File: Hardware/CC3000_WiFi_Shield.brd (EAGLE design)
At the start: 66 x 53.3 mm, 37 parts, among them J1 U.FL, U2 ARDUINO_SHIELDNOLABELS, U3 74HC4050, U4 USD-SOCKETNEW, U5 CC3000, U6 74AHC1G125

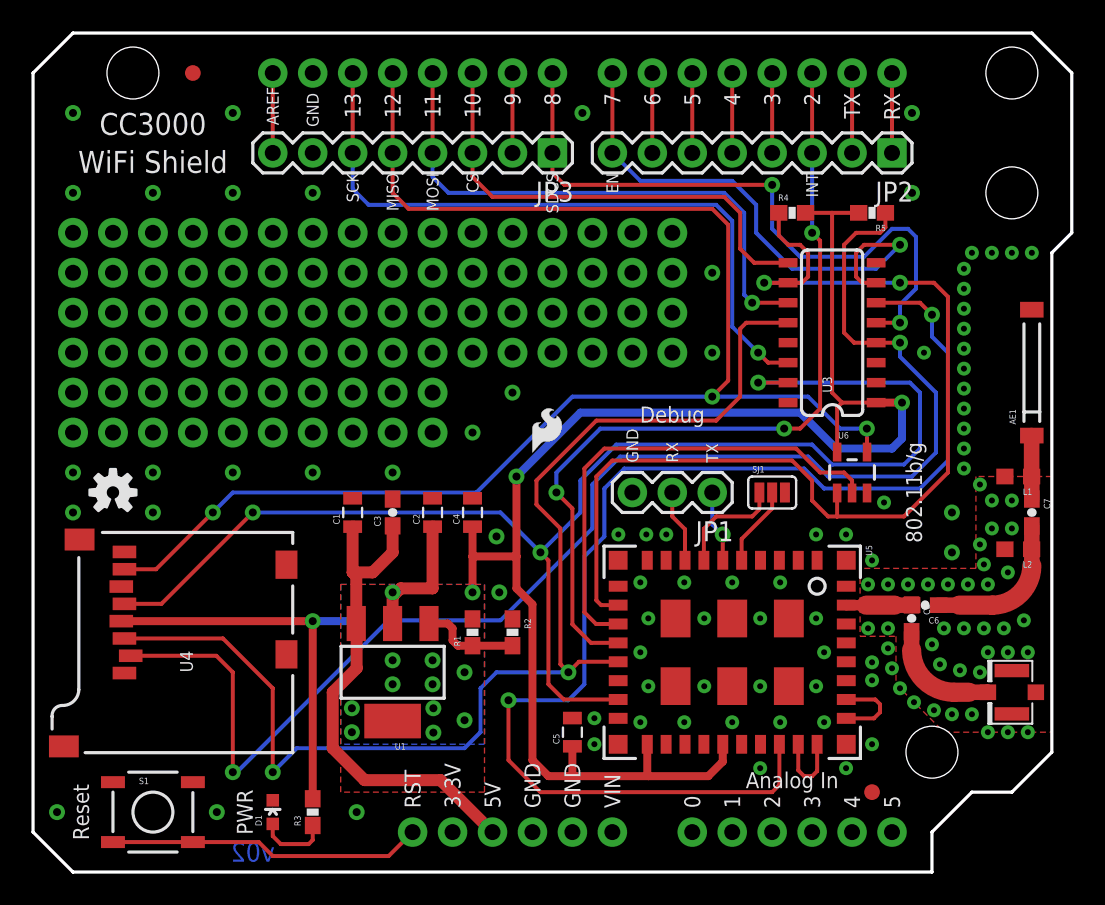
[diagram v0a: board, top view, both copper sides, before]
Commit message: Added power breakout near proto area. Removed silk from shield headers. Changed silk text to 0.032 in. size. Added ISP headers to work with Leonardo. Added 10-pin shield headers to work woth UNO R3. Adjusted notch on bottom-right corner of board.
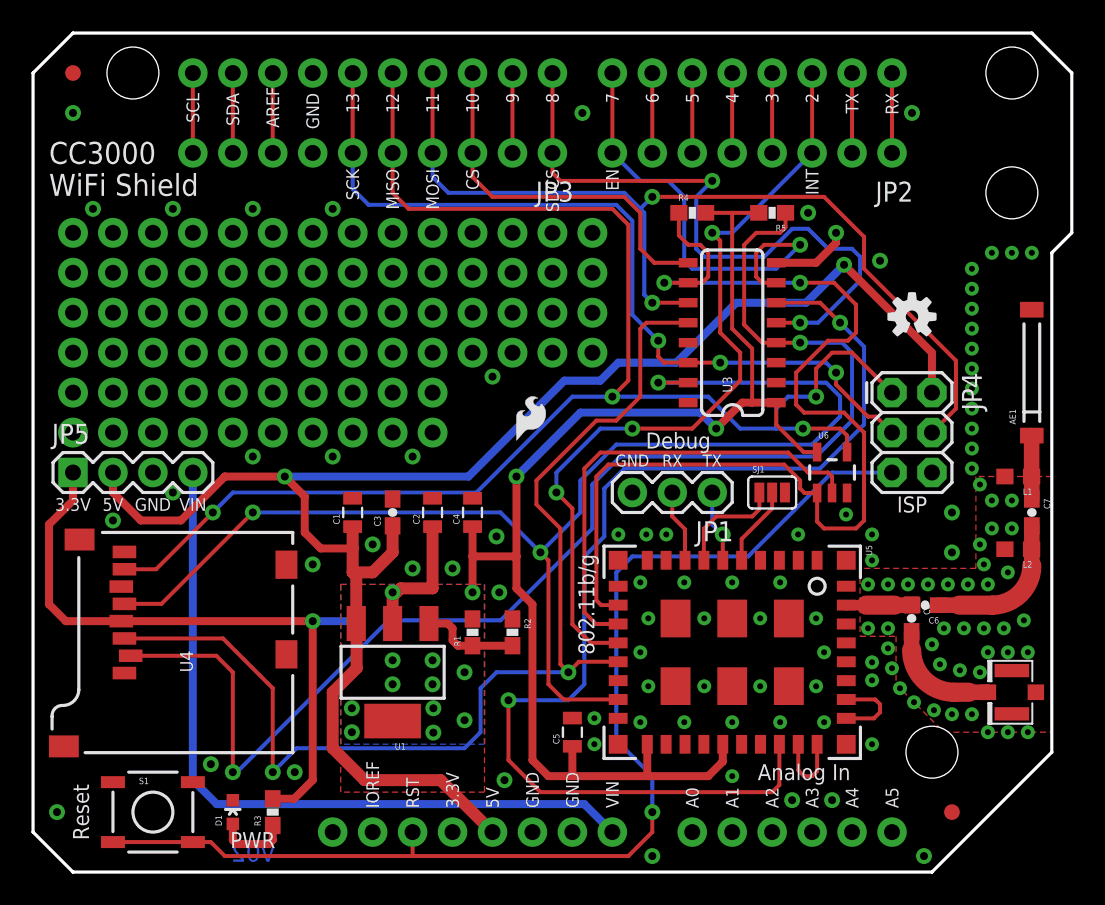
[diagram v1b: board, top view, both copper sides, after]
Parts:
- added JP4: AVR_SPI_PRG_6PTH, SparkFun-Connectors:2X3
- added JP5: (no value), SparkFun-Connectors:1X04
- JP2: device SparkFun-Connectors:1X08 -> SparkFun-Connectors:1X08_NO_SILK
- JP3: value (none) -> M10NO_SILK; device SparkFun-Connectors:1X08 -> SparkFun-Connectors:1X10_NO_SILK
- U2: value ARDUINO_SHIELDNOLABELS -> ARDUINO_R3_SHIELDNOLABELS; device SparkFun-Boards:DUEMILANOVE_SHIELD_NOLABELS -> SparkFun-Boards:UNO_R3_SHIELD_NOLABELS
- moved LOGO1 52.0 mm to (55.9, 35.3)
- moved FID2 7.62 mm to (2.54, 50.8)
- moved R4 6.35 mm to (41.9, 41.9)
- moved R5 6.35 mm to (47.0, 41.9)
- moved U3 6.35 mm to (44.5, 34.3)
- moved FID1 5.24 mm to (58.4, 3.81)
- moved D1 2.54 mm to (12.7, 3.81)
- moved R3 2.54 mm to (15.2, 3.81)
- moved U6 1.27 mm to (50.8, 25.4)
- moved LOGO3 1.27 mm to (30.7, 27.4)
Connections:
- removed net N$1: S1.3, S1.4, U2.RES
- new net RESET: JP4.5, S1.3, S1.4, U2.RES
- new net SCL: JP3.10, U2.SCL
- new net SDA: JP3.9, U2.SDA
- new net VIN: JP5.4, U2.VIN
- net 3.3V: now also JP5.1
- net 5V: now also JP4.2, JP5.2
- net GND: now also JP4.6, JP5.3
- net MISO_3.3V: now also JP4.1
- net MOSI_5V: now also JP4.4
- net SCK_5V: now also JP4.3
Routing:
- net RESET: track 0.00 -> 74.4 mm, vias 0 -> 1
- net 5V: track 31.9 -> 105.2 mm, vias 0 -> 2
- net VIN: track 0.00 -> 47.6 mm
- net MOSI_5V: track 35.6 -> 60.3 mm, vias 1 -> 2
- net N$1: track 20.0 -> 0.00 mm
- net SCK_5V: track 43.7 -> 52.8 mm, vias 1 -> 3
- net EN_3.3V: track 80.1 -> 72.8 mm
- net CS_5V: track 30.3 -> 23.9 mm
- net MOSI_3.3V: track 78.3 -> 71.9 mm
- net SCK_3.3V: track 88.4 -> 82.2 mm
- net SD_CS_3.3V: track 90.4 -> 84.5 mm
- net SDA: track 0.00 -> 5.08 mm
- net SCL: track 0.00 -> 5.08 mm
- net EN_5V: track 34.1 -> 29.0 mm
- net GND: track 0.00 -> 4.97 mm, vias 115 -> 117
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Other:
- outline, holes or cut-outs redrawn
- board text added: "A0"
- board text added: "A1"
- board text added: "A2"
- board text added: "A3"
- board text added: "A4"
- board text added: "A5"
- board text added: "IOREF"
- board text added: "ISP"
- board text added: "SCL"
- board text added: "SDA"
- board text removed: "0"
- board text removed: "1"

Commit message: Moved ext antenna mount back 50 mil; re-routed SD_CS line to avoid splitting power plane on bottom; Added 'Antenna Select' to SS; Added SS marker to U.FL; Added 'Mode' in SS to jumper; Changed to v10
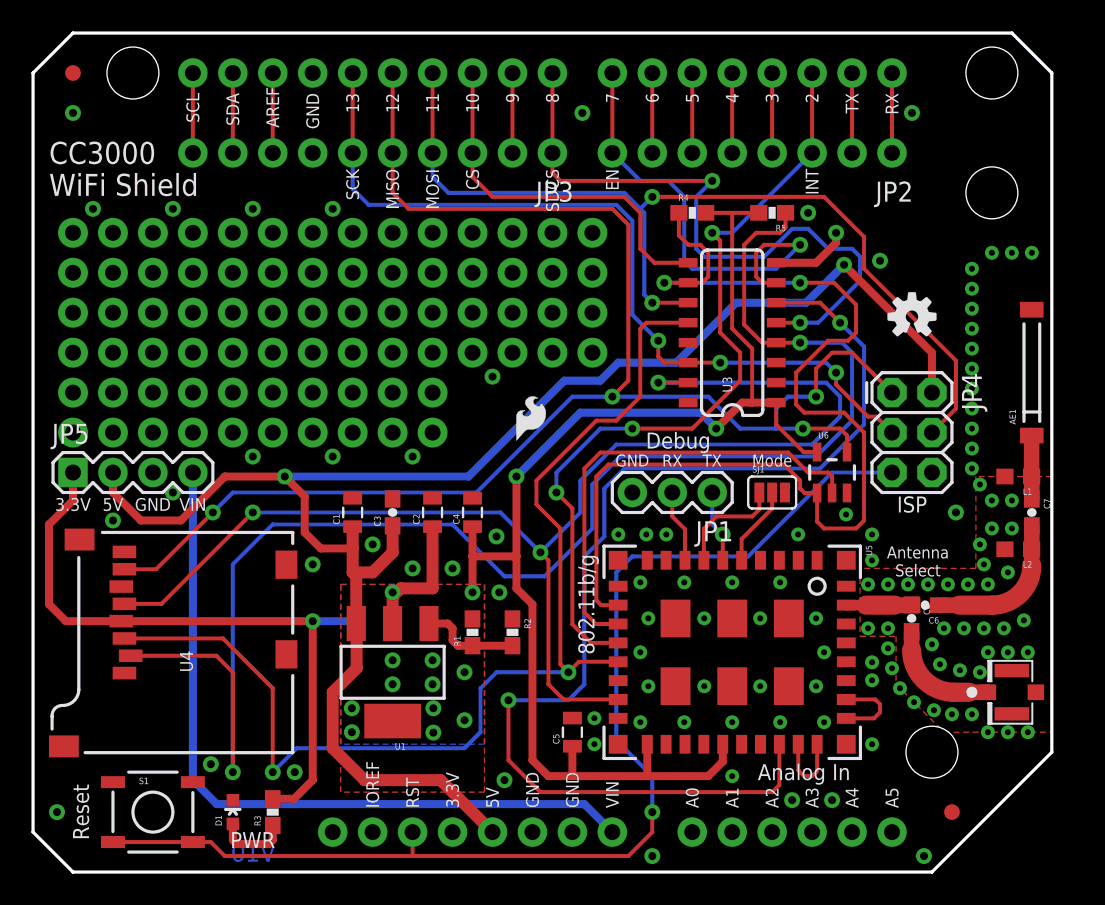
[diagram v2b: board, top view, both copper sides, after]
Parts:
- moved STANDOFF1 1.27 mm to (61.0, 50.8)
- moved STANDOFF2 1.27 mm to (61.0, 43.2)
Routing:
- net SD_CS_3.3V: track 84.5 -> 95.0 mm
- net GND: vias 117 -> 116
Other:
- board size 66 x 53.3 mm -> 64.8 x 53.3 mm
- board text added: "Antenna Select"
- board text added: "Mode"
- board text added: "v10"
- board text removed: "v02"
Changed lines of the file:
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@@
 <setting verticaltext="up"/>
 </settings>
-<grid distance="0.05" unitdist="inch" unit="inch" style="dots" multiple="1" display="yes" altdistance="0.005" altunitdist="inch" altunit="inch"/>
+<grid distance="0.01" unitdist="inch" unit="inch" style="dots" multiple="1" display="yes" altdistance="0.005" altunitdist="inch" altunit="inch"/>
 <layers>
 <layer number="1" name="Top" color="4" fill="1" visible="yes" active="yes"/>
 <layer number="2" name="Route2" color="1" fill="3" visible="no" active="yes"/>
 <layer number="15" name="Route15" color="4" fill="6" visible="no" active="yes"/>
-<layer number="16" name="Bottom" color="1" fill="1" visible="no" active="yes"/>
+<layer number="16" name="Bottom" color="1" fill="1" visible="yes" active="yes"/>
 <layer number="17" name="Pads" color="2" fill="1" visible="yes" active="yes"/>
 <layer number="18" name="Vias" color="2" fill="1" visible="yes" active="yes"/>
@@
 <layer number="20" name="Dimension" color="15" fill="1" visible="yes" active="yes"/>
 <layer number="21" name="tPlace" color="16" fill="1" visible="yes" active="yes"/>
-<layer number="22" name="bPlace" color="14" fill="1" visible="no" active="yes"/>
+<layer number="22" name="bPlace" color="14" fill="1" visible="yes" active="yes"/>
 <layer number="23" name="tOrigins" color="15" fill="1" visible="yes" active="yes"/>
-<layer number="24" name="bOrigins" color="15" fill="1" visible="no" active="yes"/>
+<layer number="24" name="bOrigins" color="15" fill="1" visible="yes" active="yes"/>
 <layer number="25" name="tNames" color="7" fill="1" visible="no" active="yes"/>
 <layer number="26" name="bNames" color="7" fill="1" visible="no" active="yes"/>
@@
 <layer number="43" name="vRestrict" color="2" fill="10" visible="no" active="yes"/>
 <layer number="44" name="Drills" color="7" fill="1" visible="no" active="yes"/>
-<layer number="45" name="Holes" color="7" fill="1" visible="no" active="yes"/>
+<layer number="45" name="Holes" color="7" fill="1" visible="yes" active="yes"/>
 <layer number="46" name="Milling" color="3" fill="1" visible="no" active="yes"/>
-<layer number="51" name="tDocu" color="6" fill="1" visible="no" active="yes"/>
+<layer number="51" name="tDocu" color="6" fill="1" visible="yes" active="yes"/>
 <layer number="52" name="bDocu" color="7" fill="1" visible="no" active="yes"/>
 <layer number="3" name="Route3" color="4" fill="3" visible="no" active="no"/>
@@
 <wire x1="0" y1="2.54" x2="0" y2="50.8" width="0.2032" layer="20"/>
 <wire x1="0" y1="50.8" x2="2.54" y2="53.34" width="0.2032" layer="20"/>
-<wire x1="2.54" y1="53.34" x2="63.5" y2="53.34" width="0.2032" layer="20"/>
-<wire x1="63.5" y1="53.34" x2="66.04" y2="50.8" width="0.2032" layer="20"/>
-<wire x1="64.77" y1="39.37" x2="64.77" y2="7.62" width="0.2032" layer="20"/>
+<wire x1="2.54" y1="53.34" x2="62.23" y2="53.34" width="0.2032" layer="20"/>
+<wire x1="62.23" y1="53.34" x2="64.77" y2="50.8" width="0.2032" layer="20"/>
+<wire x1="64.77" y1="50.8" x2="64.77" y2="7.62" width="0.2032" layer="20"/>
 <wire x1="64.77" y1="7.62" x2="57.15" y2="0" width="0.2032" layer="20"/>
 <wire x1="57.15" y1="0" x2="2.54" y2="0" width="0.2032" layer="20"/>
 <wire x1="2.54" y1="0" x2="0" y2="2.54" width="0.2032" layer="20"/>
-<wire x1="66.04" y1="40.64" x2="64.77" y2="39.37" width="0.2032" layer="20"/>
-<wire x1="66.04" y1="50.8" x2="66.04" y2="40.64" width="0.2032" layer="20"/>
 <rectangle x1="61.468" y1="10.668" x2="62.992" y2="12.192" layer="41"/>
 <text x="20.32" y="44.704" size="0.8128" layer="21" font="vector" ratio="15" rot="R90" align="center-right">SCK</text>
@@
 <text x="41.021" y="26.924" size="1.016" layer="21" font="vector" ratio="15" align="bottom-center">Debug</text>
 <text x="31.75" y="-16.51" size="1.778" layer="51" font="vector">Shawn Hymel</text>
-<text x="13.97" y="1.27" size="1.2192" layer="16" font="vector" ratio="15" rot="MR0" align="center">v02</text>
+<text x="13.97" y="1.27" size="1.2192" layer="16" font="vector" ratio="15" rot="MR0" align="center">v10</text>
 <text x="1.016" y="45.72" size="1.397" layer="21" font="vector" ratio="15" align="center-left">CC3000</text>
 <text x="1.016" y="43.688" size="1.397" layer="21" font="vector" ratio="15" align="center-left">WiFi Shield</text>
@@
 <rectangle x1="62.484" y1="28.448" x2="64.262" y2="35.052" layer="41"/>
 <rectangle x1="60.452" y1="25.908" x2="64.262" y2="38.608" layer="42"/>
+<circle x="59.69" y="11.43" radius="0.179603125" width="0.3556" layer="21"/>
+<text x="56.261" y="18.796" size="0.762" layer="21" font="vector" ratio="15" align="bottom-center">Antenna
+Select</text>
+<text x="46.99" y="26.162" size="0.762" layer="21" font="vector" ratio="15" align="center">Mode</text>
 </plain>
 <attributes>
@@
 <element name="JP2" library="SparkFun-Connectors" package="1X08_NO_SILK" value="" x="54.61" y="45.72" rot="R180"/>
 <element name="JP3" library="SparkFun-Connectors" package="1X10_NO_SILK" value="M10NO_SILK" x="33.02" y="45.72" rot="R180"/>
-<element name="STANDOFF1" library="SparkFun-Electromechanical" package="STAND-OFF" value="STAND-OFF" x="62.23" y="50.8"/>
-<element name="STANDOFF2" library="SparkFun-Electromechanical" package="STAND-OFF" value="STAND-OFF" x="62.23" y="43.18"/>
+<element name="STANDOFF1" library="SparkFun-Electromechanical" package="STAND-OFF" value="STAND-OFF" x="60.96" y="50.8"/>
+<element name="STANDOFF2" library="SparkFun-Electromechanical" package="STAND-OFF" value="STAND-OFF" x="60.96" y="43.18"/>
 <element name="JP4" library="SparkFun-Connectors" package="2X3" value="AVR_SPI_PRG_6PTH" x="54.61" y="30.48" rot="R270"/>
 <element name="JP5" library="SparkFun-Connectors" package="1X04" value="" x="2.54" y="25.4"/>
@@
 <vertex x="0" y="50.8"/>
 <vertex x="2.54" y="53.34"/>
-<vertex x="63.5" y="53.34"/>
-<vertex x="66.04" y="50.8"/>
-<vertex x="66.04" y="40.64"/>
-<vertex x="64.77" y="39.37"/>
+<vertex x="62.23" y="53.34"/>
+<vertex x="64.77" y="50.8"/>
 <vertex x="64.77" y="7.62"/>
 <vertex x="57.15" y="0"/>
@@
 <vertex x="0" y="50.8"/>
 <vertex x="2.54" y="53.34"/>
-<vertex x="63.5" y="53.34"/>
-<vertex x="66.04" y="50.8"/>
-<vertex x="66.04" y="40.64"/>
-<vertex x="64.77" y="39.37"/>
+<vertex x="62.23" y="53.34"/>
+<vertex x="64.77" y="50.8"/>
 <vertex x="64.77" y="7.62"/>
 <vertex x="57.15" y="0"/>
@@
 <via x="35.687" y="8.128" extent="1-16" drill="0.381"/>
 <via x="35.687" y="9.779" extent="1-16" drill="0.381"/>
-<via x="58.42" y="20.32" extent="1-16" drill="0.508"/>
-<via x="58.42" y="22.86" extent="1-16" drill="0.508"/>
+<via x="58.674" y="22.86" extent="1-16" drill="0.508"/>
 <via x="1.524" y="3.81" extent="1-16" drill="0.508"/>
 <via x="13.97" y="42.164" extent="1-16" drill="0.508"/>
@@
 <wire x1="11.65" y1="13.75" x2="12.7" y2="12.7" width="0.254" layer="1"/>
 <wire x1="12.7" y1="12.7" x2="12.7" y2="6.35" width="0.254" layer="1"/>
-<wire x1="12.7" y1="6.35" x2="12.954" y2="6.35" width="0.254" layer="16"/>
-<wire x1="12.954" y1="6.35" x2="22.606" y2="16.002" width="0.254" layer="16"/>
 <via x="48.768" y="33.655" extent="1-16" drill="0.508"/>
 <wire x1="35.56" y1="24.638" x2="35.56" y2="21.844" width="0.254" layer="16"/>
-<wire x1="22.606" y1="16.002" x2="29.718" y2="16.002" width="0.254" layer="16"/>
-<wire x1="29.718" y1="16.002" x2="35.56" y2="21.844" width="0.254" layer="16"/>
 <wire x1="35.56" y1="24.638" x2="37.338" y2="26.416" width="0.254" layer="16"/>
 <wire x1="37.338" y1="26.416" x2="49.784" y2="26.416" width="0.254" layer="16"/>
@@
 <wire x1="52.07" y1="28.702" x2="52.07" y2="33.02" width="0.254" layer="16"/>
 <wire x1="51.435" y1="33.655" x2="52.07" y2="33.02" width="0.254" layer="16"/>
+<wire x1="35.56" y1="21.844" x2="32.512" y2="18.796" width="0.254" layer="16"/>
+<wire x1="32.512" y1="18.796" x2="29.972" y2="18.796" width="0.254" layer="16"/>
+<wire x1="29.972" y1="18.796" x2="26.67" y2="22.098" width="0.254" layer="16"/>
+<wire x1="26.67" y1="22.098" x2="15.24" y2="22.098" width="0.254" layer="16"/>
+<wire x1="12.7" y1="6.35" x2="12.7" y2="19.558" width="0.254" layer="16"/>
+<wire x1="12.7" y1="19.558" x2="15.24" y2="22.098" width="0.254" layer="16"/>
 </signal>
 <signal name="SDA">
@@
 </board>
 </drawing>
+<compatibility>
+<note version="6.3" minversion="6.2.2" severity="warning">
+Since Version 6.2.2 text objects can contain more than one line,
+which will not be processed correctly with this version.
+</note>
+</compatibility>
 </eagle>

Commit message: Added silk U.FL; Adjusted tvalue markings for easier reading
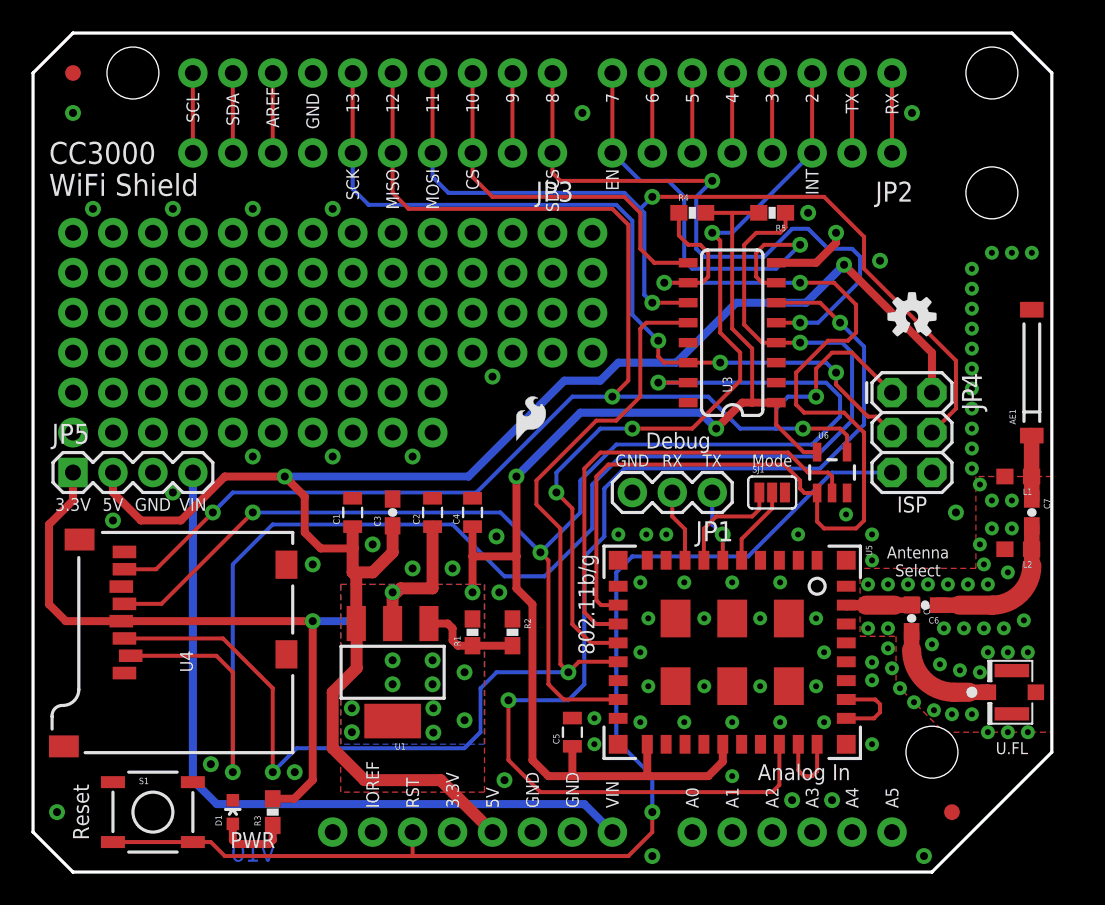
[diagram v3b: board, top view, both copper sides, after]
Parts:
- L1: value (none) -> DNP
- U1: value (none) -> LM1117
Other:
- board text added: "U.FL"
